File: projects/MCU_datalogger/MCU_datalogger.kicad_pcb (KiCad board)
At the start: 2 copper layers, 50.8 x 35.5 mm, 33 parts, among them J1 Conn_01x04_Pin, J2 Conn_01x09_Pin, J3 Conn_01x04_Pin, J4 Conn_02x03_Odd_Even, U1 24LC1025, U2 DS1337S_, U3 24LC1025, U4 ATMEGA328P-AU, Y1 32.768KHz, Y2 16MHz

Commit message: MCU datalogger v1.2 (2-layer) - update PBC from schematic to bring /MH net label
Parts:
- removed REF**: KiCad-Logo2_5mm_SilkScreen, Symbol:KiCad-Logo2_5mm_SilkScreen
- removed REF**: KiCad-Logo2_5mm_Copper, Symbol:KiCad-Logo2_5mm_Copper
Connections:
- net Net-(U4-AREF) renamed /MH

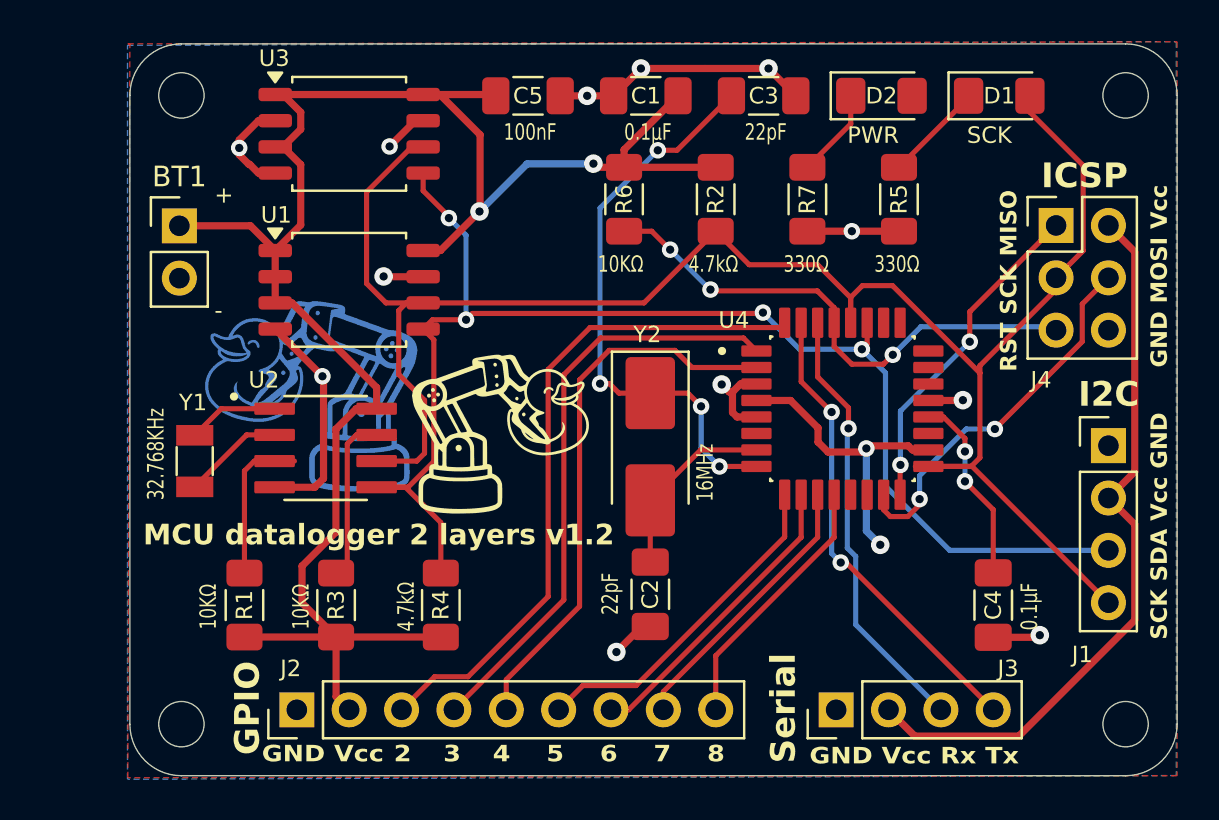
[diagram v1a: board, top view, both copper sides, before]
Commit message: MCU datalogger v1.3 (2-layer) complete - fixes SCL/SCK bug
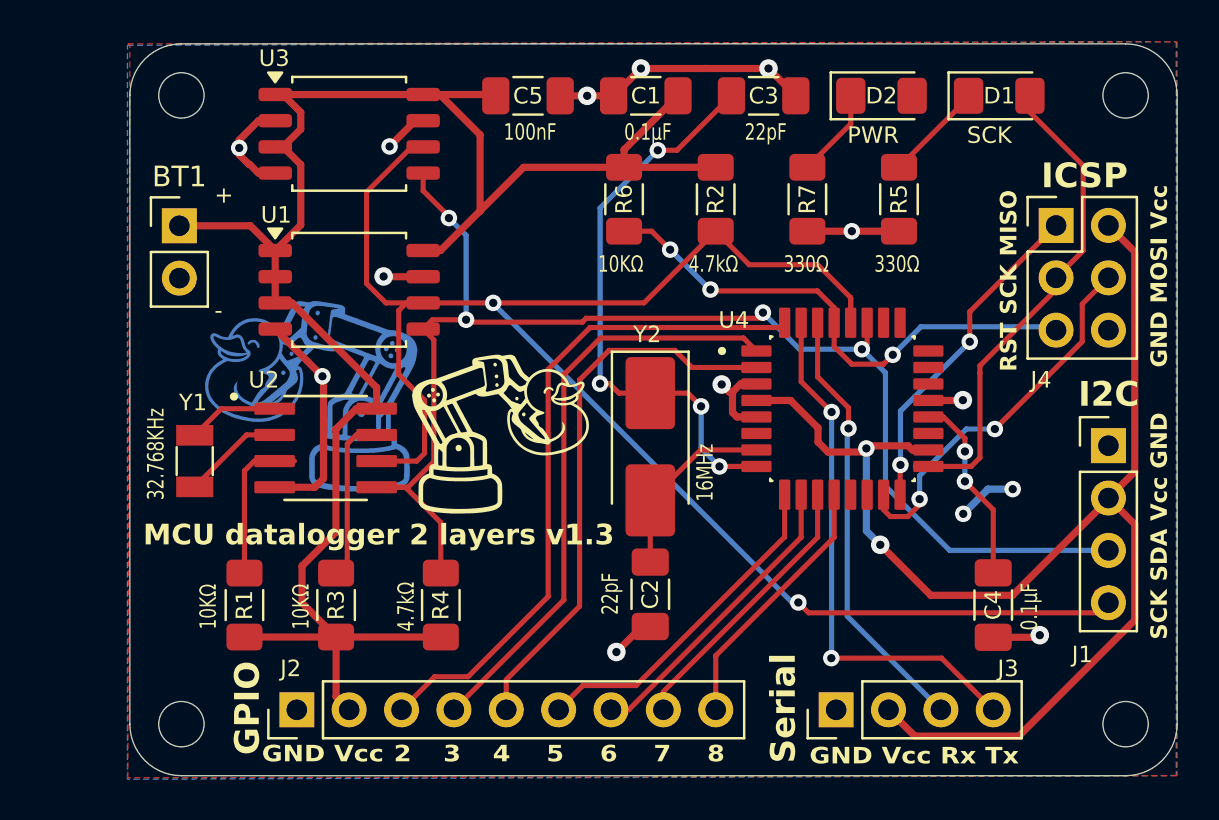
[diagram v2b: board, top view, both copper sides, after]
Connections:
- J1 pad 4: /SCK -> /SCL
- R2 pad 2: /SCK -> /SCL
- U1 pad 6: /SCK -> /SCL
- U2 pad 6: /SCK -> /SCL
- U3 pad 6: /SCK -> /SCL
- U4 pad 28: /SCK -> /SCL
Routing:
- net /SCL: track 0.00 -> 84.3 mm, vias 0 -> 2
- net /SCK: track 91.8 -> 24.0 mm
- net /Vcc: track 141.5 -> 158.3 mm
- net /TX: track 22.8 -> 25.8 mm
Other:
- board text added: "MCU datalogger 2 layers v1.3"
- board text removed: "MCU datalogger 2 layers v1.2"

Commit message: MCU datalogger v1.3 (2-layer) - silkscreen improvements, plot gerbers
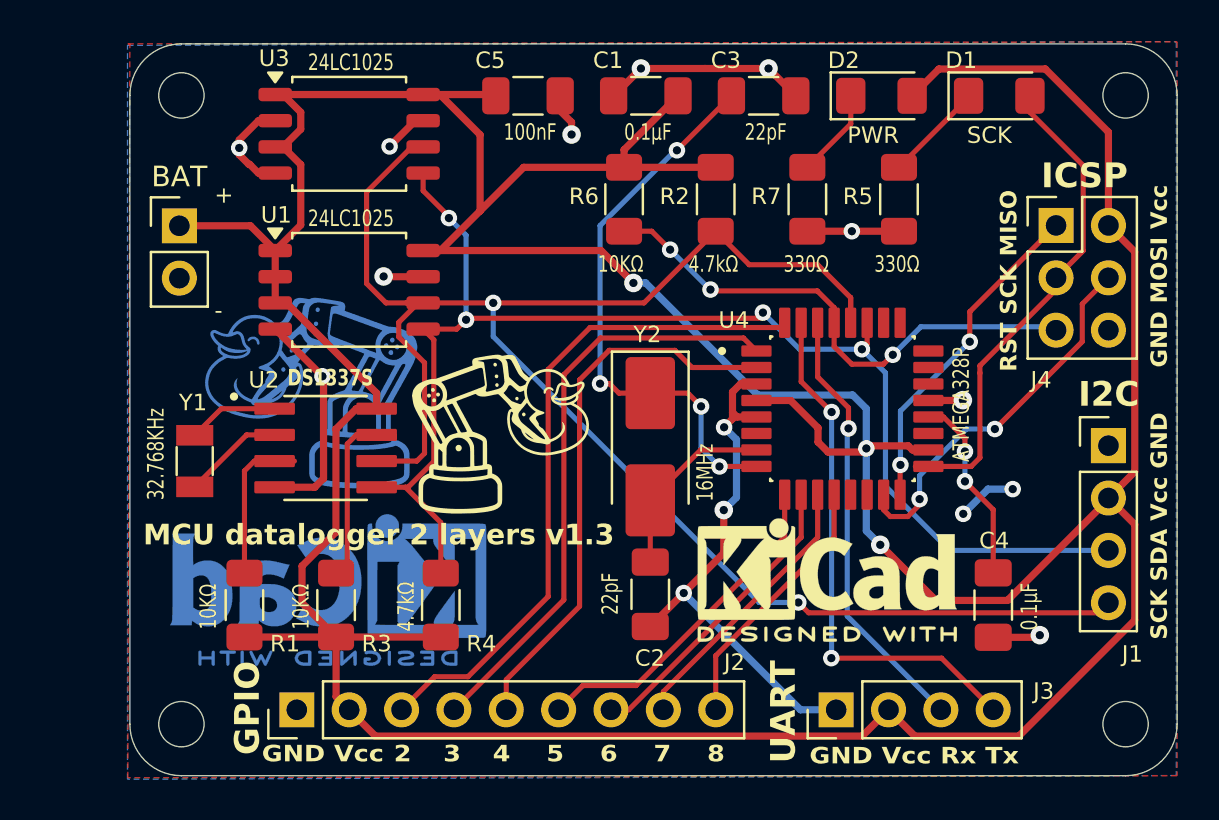
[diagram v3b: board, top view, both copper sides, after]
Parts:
- added REF**: KiCad-Logo2_5mm_SilkScreen, Symbol:KiCad-Logo2_5mm_SilkScreen, F.Cu at (127.6, 106.8)
- added REF**: KiCad-Logo2_6mm_Copper, Symbol:KiCad-Logo2_6mm_Copper, B.Cu at (103.4, 106.6)
- U2: value DS1337S_ -> DS1337S
- U4: value ATMEGA328P-AU -> ATMEGA328P
- moved G*** 0.16 mm to (102.7, 97.2)
- renumbered BT1 to BAT
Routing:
- net /Vcc: track 158.3 -> 228.0 mm, vias 4 -> 5
- net GND: track 47.7 -> 67.1 mm, vias 12 -> 13
- net /SCL: track 84.3 -> 85.8 mm
- net /SDA: track 65.5 -> 66.0 mm
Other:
- board text added: "UART"
- board text removed: "Serial"
